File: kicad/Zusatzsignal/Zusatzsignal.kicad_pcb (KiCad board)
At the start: 2 copper layers, 3.7 x 5.3 mm, 3 parts, among them J1 VCC, J2 Zs

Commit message: Update ZS readme
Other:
- board text added: "ZSv2"
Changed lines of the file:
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@@
 (kicad_pcb (version 20211014) (generator pcbnew)
   (general
-    (thickness 1.6)
+    (thickness 0.8)
   )
   (paper "A4")
@@
   )
   (setup
+    (stackup
+      (layer "F.SilkS" (type "Top Silk Screen"))
+      (layer "F.Paste" (type "Top Solder Paste"))
+      (layer "F.Mask" (type "Top Solder Mask") (thickness 0.01))
+      (layer "F.Cu" (type "copper") (thickness 0.035))
+      (layer "dielectric 1" (type "core") (thickness 0.71) (material "FR4") (epsilon_r 4.5) (loss_tangent 0.02))
+      (layer "B.Cu" (type "copper") (thickness 0.035))
+      (layer "B.Mask" (type "Bottom Solder Mask") (thickness 0.01))
+      (layer "B.Paste" (type "Bottom Solder Paste"))
+      (layer "B.SilkS" (type "Bottom Silk Screen"))
+      (copper_finish "None")
+      (dielectric_constraints no)
+    )
     (pad_to_mask_clearance 0)
     (pcbplotparams
@@
     (effects (font (size 1 1) (thickness 0.15)) (justify mirror))
   )
+  (gr_text "ZSv2" (at 139.8 83.6) (layer "B.SilkS")
+    (effects (font (size 0.8 0.8) (thickness 0.15)) (justify mirror))
+  )
   (segment (start 140.6875 81.967785) (end 140.6875 81.6) (width 0.25) (layer "F.Cu") (net 1))

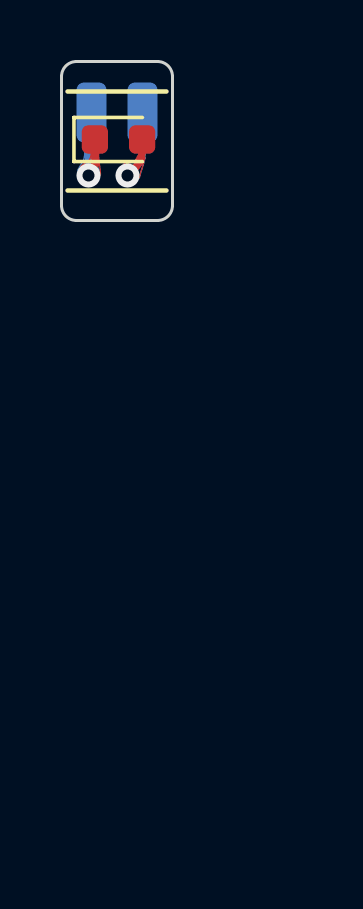
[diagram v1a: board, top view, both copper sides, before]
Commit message: feat: Change ZS to use 0403 LED
Try production step with same LEDs as used on the main signals.
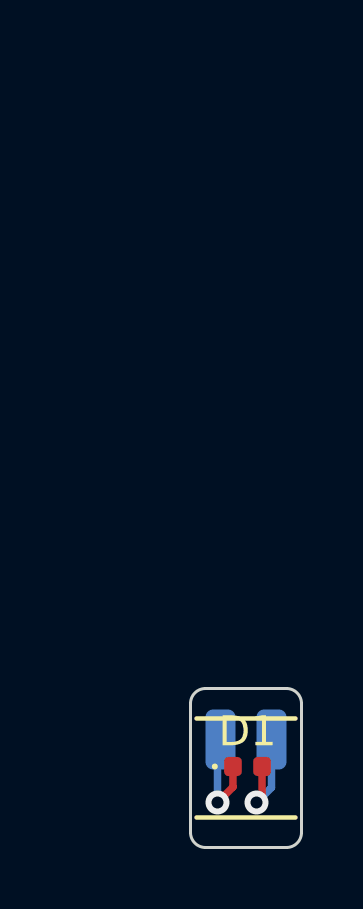
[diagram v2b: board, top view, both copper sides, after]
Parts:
- D1: footprint LED_SMD:LED_0603_1608Metric -> LED_SMD:LED_0402_1005Metric
- moved D1 21.3 mm to (144.2, 102.5)
- moved J1 21.3 mm to (145.0, 101.6)
- moved J2 21.3 mm to (143.3, 101.6)
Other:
- board text added: "ZSv3"
- board text removed: "ZSv2"

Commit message: Add CC-BY-SA 4.0 license
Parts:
- moved D1 58.8 mm to (98.4, 65.6)
- moved J2 58.8 mm to (97.5, 64.7)
- moved J1 58.8 mm to (99.2, 64.7)
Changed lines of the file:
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@@
     (thickness 0.8)
   )
-  (paper "A4")
+  (paper "A5")
   (title_block
-    (title "ZS")
+    (title "KS-Zusatzsignal")
+    (date "2023-12-17")
     (rev "v3")
-    (comment 4 "AISLER Project ID: DXIHIPTI")
   )
   (layers
@@
     )
     (pad_to_mask_clearance 0)
+    (aux_axis_origin 96.5 63)
     (pcbplotparams
       (layerselection 0x00010fc_ffffffff)
@@
   (net 2 "Net-(D1-Pad1)")
   (footprint "LED_SMD:LED_0402_1005Metric" (layer "F.Cu")
-    (at 144.2 102.5)
+    (at 98.4 65.6)
     (descr "LED SMD 0402 (1005 Metric), square (rectangular) end terminal, IPC_7351 nominal, (Body size source: http://www.tortai-tech.com/upload/download/2011102023233369053.pdf), generated with kicad-footprint-generator")
     (tags "LED")
@@
   )
   (footprint "Connector_Wire:SolderWirePad_1x01_SMD_1x2mm" (layer "B.Cu")
-    (at 143.3 101.6 180)
+    (at 97.5 64.7 180)
     (descr "Wire Pad, Square, SMD Pad,  5mm x 10mm,")
     (tags "MesurementPoint Square SMDPad 5mmx10mm ")
@@
   )
   (footprint "Connector_Wire:SolderWirePad_1x01_SMD_1x2mm" (layer "B.Cu")
-    (at 145 101.6 180)
+    (at 99.2 64.7 180)
     (descr "Wire Pad, Square, SMD Pad,  5mm x 10mm,")
     (tags "MesurementPoint Square SMDPad 5mmx10mm ")
@@
       (net 1 "Net-(D1-Pad2)") (pinfunction "Pin_1") (pintype "passive"))
   )
-  (gr_line (start 145.8 100.9) (end 142.5 100.9)
+  (gr_line (start 100 64) (end 96.7 64)
     (stroke (width 0.15) (type solid)) (layer "F.SilkS"))
-  (gr_line (start 145.8 104.2) (end 142.5 104.2)
+  (gr_line (start 100 67.3) (end 96.7 67.3)
     (stroke (width 0.15) (type solid)) (layer "F.SilkS"))
-  (gr_line (start 142.8 99.9) (end 145.5 99.9)
-    (stroke (width 0.1) (type solid)) (layer "Edge.Cuts"))
-  (gr_arc (start 142.3 100.4) (mid 142.446447 100.046447) (end 142.8 99.9)
-    (stroke (width 0.1) (type solid)) (layer "Edge.Cuts"))
-  (gr_line (start 146 100.4) (end 146 104.7)
-    (stroke (width 0.1) (type solid)) (layer "Edge.Cuts"))
-  (gr_line (start 142.3 104.7) (end 142.3 100.4)
-    (stroke (width 0.1) (type solid)) (layer "Edge.Cuts"))
-  (gr_arc (start 145.5 99.9) (mid 145.853553 100.046447) (end 146 100.4)
-    (stroke (width 0.1) (type solid)) (layer "Edge.Cuts"))
-  (gr_arc (start 146 104.7) (mid 145.853553 105.053553) (end 145.5 105.2)
-    (stroke (width 0.1) (type solid)) (layer "Edge.Cuts"))
-  (gr_line (start 145.5 105.2) (end 142.8 105.2)
-    (stroke (width 0.1) (type solid)) (layer "Edge.Cuts"))
-  (gr_arc (start 142.8 105.2) (mid 142.446447 105.053553) (end 142.3 104.7)
-    (stroke (width 0.1) (type solid)) (layer "Edge.Cuts"))
-  (gr_text "+" (at 145 103.1) (layer "B.SilkS")
+  (gr_line (start 97 63) (end 99.7 63)
+    (stroke (width 0.1) (type solid)) (layer "Edge.Cuts"))
+  (gr_arc (start 96.5 63.5) (mid 96.646447 63.146447) (end 97 63)
+    (stroke (width 0.1) (type solid)) (layer "Edge.Cuts"))
+  (gr_line (start 100.2 63.5) (end 100.2 67.8)
+    (stroke (width 0.1) (type solid)) (layer "Edge.Cuts"))
+  (gr_line (start 96.5 67.8) (end 96.5 63.5)
+    (stroke (width 0.1) (type solid)) (layer "Edge.Cuts"))
+  (gr_arc (start 99.7 63) (mid 100.053553 63.146447) (end 100.2 63.5)
+    (stroke (width 0.1) (type solid)) (layer "Edge.Cuts"))
+  (gr_arc (start 100.2 67.8) (mid 100.053553 68.153553) (end 99.7 68.3)
+    (stroke (width 0.1) (type solid)) (layer "Edge.Cuts"))
+  (gr_line (start 99.7 68.3) (end 97 68.3)
+    (stroke (width 0.1) (type solid)) (layer "Edge.Cuts"))
+  (gr_arc (start 97 68.3) (mid 96.646447 68.153553) (end 96.5 67.8)
+    (stroke (width 0.1) (type solid)) (layer "Edge.Cuts"))
+  (gr_text "+" (at 99.2 66.2) (layer "B.SilkS")
     (effects (font (size 1 1) (thickness 0.15)) (justify mirror))
   )
-  (gr_text "ZSv3" (at 144.1 104.5) (layer "B.SilkS")
+  (gr_text "ZSv3" (at 98.3 67.6) (layer "B.SilkS")
     (effects (font (size 0.8 0.8) (thickness 0.15)) (justify mirror))
   )
-  (segment (start 144.685 102.5) (end 144.685 103.515) (width 0.25) (layer "F.Cu") (net 1))
-  (segment (start 144.685 103.515) (end 144.5 103.7) (width 0.25) (layer "F.Cu") (net 1))
-  (via (at 144.5 103.7) (size 0.8) (drill 0.4) (layers "F.Cu" "B.Cu") (net 1))
-  (segment (start 145 101.6) (end 145 103.2) (width 0.25) (layer "B.Cu") (net 1))
-  (segment (start 145 103.2) (end 144.5 103.7) (width 0.25) (layer "B.Cu") (net 1))
-  (segment (start 143.715 103.185) (end 143.2 103.7) (width 0.25) (layer "F.Cu") (net 2))
-  (segment (start 143.715 102.5) (end 143.715 103.185) (width 0.25) (layer "F.Cu") (net 2))
-  (via (at 143.2 103.7) (size 0.8) (drill 0.4) (layers "F.Cu" "B.Cu") (net 2))
-  (segment (start 143.2 103.7) (end 143.2 101.7) (width 0.25) (layer "B.Cu") (net 2))
-  (segment (start 143.2 101.7) (end 143.3 101.6) (width 0.25) (layer "B.Cu") (net 2))
-  (segment (start 143.25 101.65) (end 143.3 101.6) (width 0.25) (layer "B.Cu") (net 2))
-  (arc (start 143.25 101.65) (mid 143.212994 101.705382) (end 143.2 101.77071) (width 0.25) (layer "B.Cu") (net 2))
+  (segment (start 98.885 65.6) (end 98.885 66.615) (width 0.25) (layer "F.Cu") (net 1))
+  (segment (start 98.885 66.615) (end 98.7 66.8) (width 0.25) (layer "F.Cu") (net 1))
+  (via (at 98.7 66.8) (size 0.8) (drill 0.4) (layers "F.Cu" "B.Cu") (net 1))
+  (segment (start 99.2 64.7) (end 99.2 66.3) (width 0.25) (layer "B.Cu") (net 1))
+  (segment (start 99.2 66.3) (end 98.7 66.8) (width 0.25) (layer "B.Cu") (net 1))
+  (segment (start 97.915 66.285) (end 97.4 66.8) (width 0.25) (layer "F.Cu") (net 2))
+  (segment (start 97.915 65.6) (end 97.915 66.285) (width 0.25) (layer "F.Cu") (net 2))
+  (via (at 97.4 66.8) (size 0.8) (drill 0.4) (layers "F.Cu" "B.Cu") (net 2))
+  (segment (start 97.4 66.8) (end 97.4 64.8) (width 0.25) (layer "B.Cu") (net 2))
+  (segment (start 97.4 64.8) (end 97.5 64.7) (width 0.25) (layer "B.Cu") (net 2))
+  (segment (start 97.45 64.75) (end 97.5 64.7) (width 0.25) (layer "B.Cu") (net 2))
+  (arc (start 97.45 64.75) (mid 97.412994 64.805382) (end 97.4 64.87071) (width 0.25) (layer "B.Cu") (net 2))
 )
